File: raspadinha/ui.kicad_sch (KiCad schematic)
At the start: 11 parts, among them Q2 BC338, SW1 RotaryEncoder_Switch

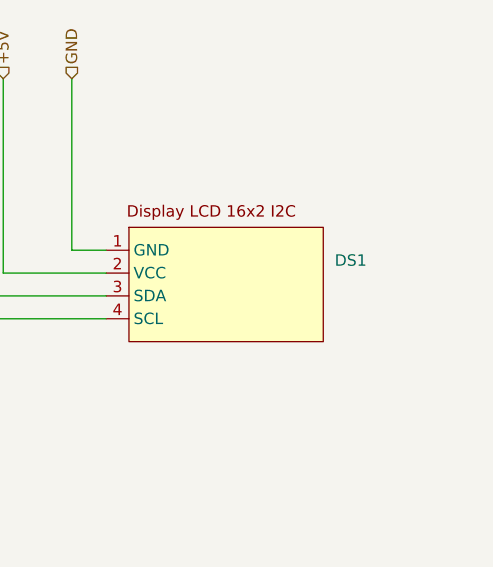
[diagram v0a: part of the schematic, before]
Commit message: feat: usando o mosfet IRFZ44N feat: switch de on/off na fonte de alimentação
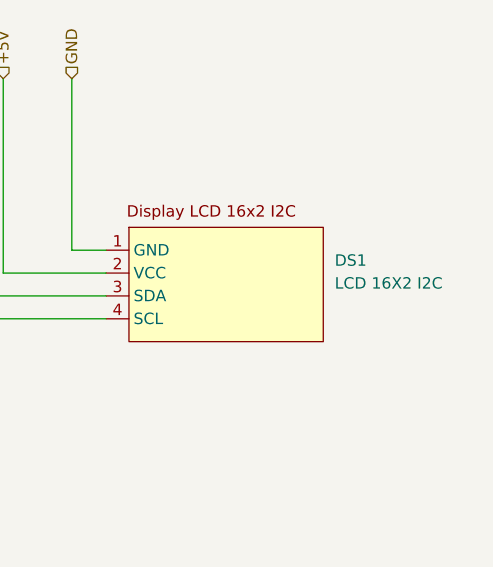
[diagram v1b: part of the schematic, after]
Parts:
- DS1: value ~ -> LCD 16X2 I2C
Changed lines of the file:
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@@
 			)
 		)
-		(property "Value" "~"
+		(property "Value" "LCD 16X2 I2C"
 			(at 248.92 83.6901 0)
 			(effects

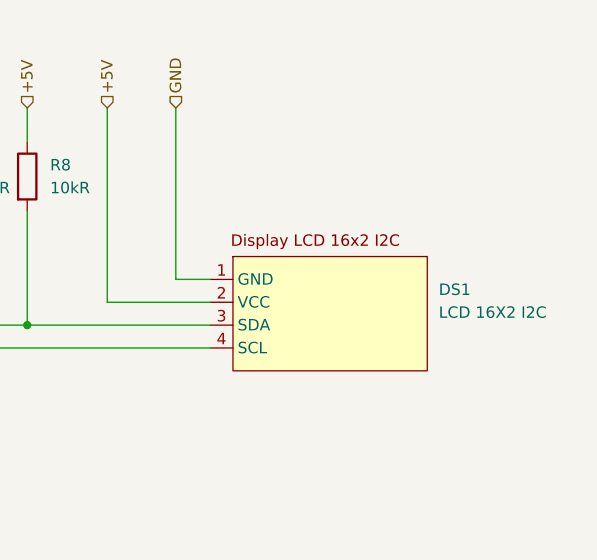
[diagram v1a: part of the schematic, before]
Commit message: feat: Mudança no display utilizado
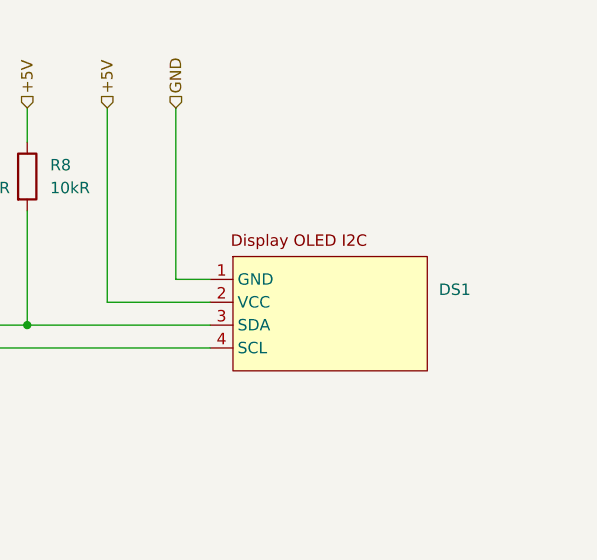
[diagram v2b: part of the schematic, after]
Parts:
- removed DS1: LCD 16X2 I2C, symbol Sorvete:Display_LCD_16x2_I2C
- added DS1: ~, symbol Sorvete:Display_OLED_I2C
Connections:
- net +5V: now also DS1.2 (VCC)
- net DISPLAY_SCL_SIGNAL: now also DS1.3 (SDA)
- net DISPLAY_SDA_SIGNAL: now also DS1.4 (SCL)
- net GND: now also DS1.1 (GND)
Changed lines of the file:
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@@
+	)
+	(symbol
+		(lib_id "Sorvete:Display_OLED_I2C")
+		(at 226.06 76.2 0)
+		(unit 1)
+		(exclude_from_sim no)
+		(in_bom yes)
+		(on_board yes)
+		(dnp no)
+		(fields_autoplaced yes)
+		(property "Reference" "DS1"
+			(at 248.92 81.1501 0)
+			(effects
+				(font
+					(size 1.27 1.27)
+				)
+				(justify left)
+			)
+		)
+		(property "Value" "~"
+			(at 248.92 83.6901 0)
+			(effects
+				(font
+					(size 1.27 1.27)
+				)
+				(justify left)
+			)
+		)
+		(property "Footprint" ""
+			(at 226.06 76.2 0)
+			(effects
+				(font
+					(size 1.27 1.27)
+				)
+				(hide yes)
+			)
+		)
+		(property "Datasheet" ""
+			(at 226.06 76.2 0)
+			(effects
+				(font
+					(size 1.27 1.27)
+				)
+				(hide yes)
+			)
+		)
+		(property "Description" ""
+			(at 226.06 76.2 0)
+			(effects
+				(font
+					(size 1.27 1.27)
+				)
+				(hide yes)
+			)
+		)
+		(pin "4"
+		)
+		(pin "3"
+		)
+		(pin "2"
+		)
+		(pin "1"
+		)
+		(instances
+			(project ""
+				(path "/0ce4bf39-76b0-428c-8682-47e2500753cc/2b8b9fc5-ba35-494d-ab10-49f62bbcd487"
+					(reference "DS1")
+					(unit 1)
+				)
+			)
+		)
 	)
 	(symbol
@@
 					(unit 1)
 				)
-			)
-		)
-	)
-	(symbol
-		(lib_id "Sorvete:Display_LCD_16x2_I2C")
-		(at 226.06 76.2 0)
-		(unit 1)
-		(exclude_from_sim no)
-		(in_bom yes)
-		(on_board yes)
-		(dnp no)
-		(fields_autoplaced yes)
-		(property "Reference" "DS1"
-			(at 248.92 81.1501 0)
-			(effects
-				(font
-					(size 1.27 1.27)
-				)
-				(justify left)
-			)
-		)
-		(property "Value" "LCD 16X2 I2C"
-			(at 248.92 83.6901 0)
-			(effects
-				(font
-					(size 1.27 1.27)
-				)
-				(justify left)
-			)
-		)
-		(property "Footprint" ""
-			(at 226.06 76.2 0)
-			(effects
-				(font
-					(size 1.27 1.27)
-				)
-				(hide yes)
-			)
-		)
-		(property "Datasheet" ""
-			(at 226.06 76.2 0)
-			(effects
-				(font
-					(size 1.27 1.27)
-				)
-				(hide yes)
-			)
-		)
-		(property "Description" ""
-			(at 226.06 76.2 0)
-			(effects
-				(font
-					(size 1.27 1.27)
-				)
-				(hide yes)
-			)
-		)
-		(pin "2"
-		)
-		(pin "3"
-		)
-		(pin "4"
-		)
-		(pin "1"
-		)
-		(instances
-			(project "raspadinha"
-				(path "/0ce4bf39-76b0-428c-8682-47e2500753cc/2b8b9fc5-ba35-494d-ab10-49f62bbcd487"
-					(reference "DS1")
-					(unit 1)
-				)

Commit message: feat: Os Footprint foram todos atribuidos fix: A placa da Esp32 foi trocada pela que temos disponível
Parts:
- BZ1: footprint (none) -> Buzzer_Beeper:MagneticBuzzer_ProSignal_ABT-410-RC
- DS1: footprint (none) -> Connector_PinHeader_2.54mm:PinHeader_1x04_P2.54mm_Vertical
- Q2: footprint (none) -> Package_TO_SOT_THT:TO-92_Inline
- R10, R11, R12, R13, R7, R8, R9: footprint (none) -> Resistor_THT:R_Axial_DIN0411_L9.9mm_D3.6mm_P12.70mm_Horizontal
- SW1: footprint (none) -> Connector_PinHeader_2.54mm:PinHeader_1x05_P2.54mm_Vertical
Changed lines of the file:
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@@
 		(title "Geladinho, UI")
 		(date "2025-11-20")
-		(rev "v1.0.0")
+		(rev "v1.1.0")
 		(company "Universidade Federal Do Ceará")
 	)
@@
 			)
 		)
-		(property "Footprint" ""
+		(property "Footprint" "Resistor_THT:R_Axial_DIN0411_L9.9mm_D3.6mm_P12.70mm_Horizontal"
 			(at 143.51 135.128 90)
 			(effects
@@
 			)
 		)
-		(property "Footprint" ""
+		(property "Footprint" "Connector_PinHeader_2.54mm:PinHeader_1x04_P2.54mm_Vertical"
 			(at 226.06 76.2 0)
 			(effects
@@
 			)
 		)
-		(property "Footprint" ""
+		(property "Footprint" "Resistor_THT:R_Axial_DIN0411_L9.9mm_D3.6mm_P12.70mm_Horizontal"
 			(at 201.422 68.58 90)
 			(effects
@@
 			)
 		)
-		(property "Footprint" ""
+		(property "Footprint" "Resistor_THT:R_Axial_DIN0411_L9.9mm_D3.6mm_P12.70mm_Horizontal"
 			(at 192.532 68.58 90)
 			(effects
@@
 			)
 		)
-		(property "Footprint" ""
+		(property "Footprint" "Package_TO_SOT_THT:TO-92_Inline"
 			(at 162.56 135.255 0)
 			(effects
@@
 			)
 		)
-		(property "Footprint" ""
+		(property "Footprint" "Resistor_THT:R_Axial_DIN0411_L9.9mm_D3.6mm_P12.70mm_Horizontal"
 			(at 132.842 142.24 90)
 			(effects
@@
 			)
 		)
-		(property "Footprint" ""
+		(property "Footprint" "Connector_PinHeader_2.54mm:PinHeader_1x05_P2.54mm_Vertical"
 			(at 93.98 78.486 0)
 			(effects
@@
 			)
 		)
-		(property "Footprint" ""
+		(property "Footprint" "Buzzer_Beeper:MagneticBuzzer_ProSignal_ABT-410-RC"
 			(at 161.925 116.84 90)
 			(effects
@@
 			)
 		)
-		(property "Footprint" ""
+		(property "Footprint" "Resistor_THT:R_Axial_DIN0411_L9.9mm_D3.6mm_P12.70mm_Horizontal"
 			(at 76.962 68.58 90)
 			(effects
@@
 			)
 		)
-		(property "Footprint" ""
+		(property "Footprint" "Resistor_THT:R_Axial_DIN0411_L9.9mm_D3.6mm_P12.70mm_Horizontal"
 			(at 66.802 68.58 90)
 			(effects
@@
 			)
 		)
-		(property "Footprint" ""
+		(property "Footprint" "Resistor_THT:R_Axial_DIN0411_L9.9mm_D3.6mm_P12.70mm_Horizontal"
 			(at 108.712 92.71 90)
 			(effects

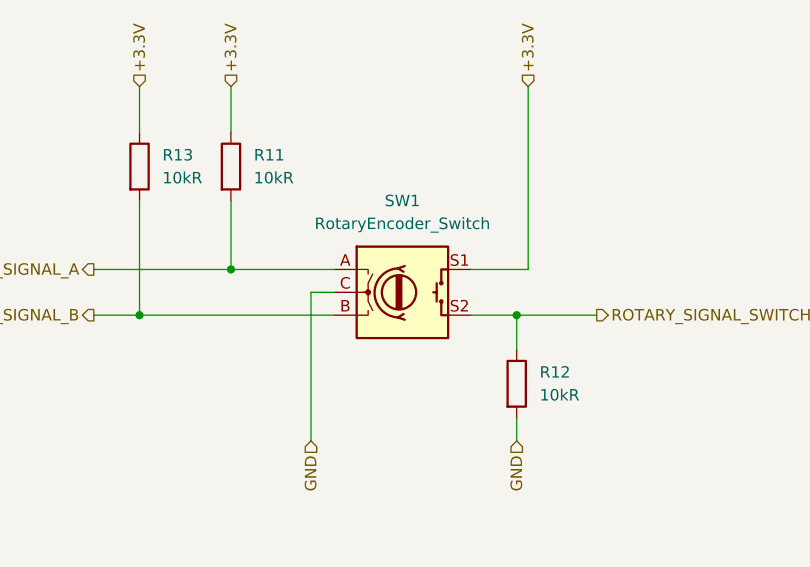
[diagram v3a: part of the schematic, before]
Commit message: feat: Posicionamento dos componentes na placa
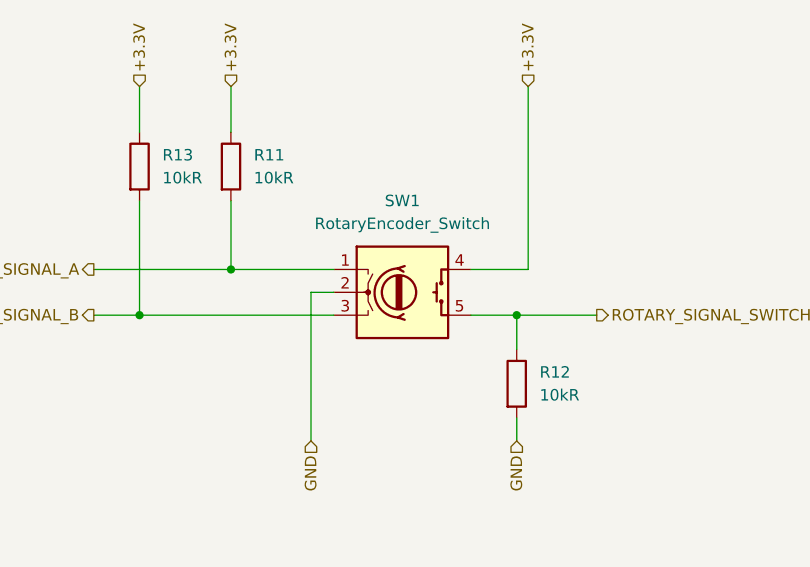
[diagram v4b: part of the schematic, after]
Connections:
- net +3.3V: now also SW1.4 (S1); no longer SW1.S1
- net GND: now also SW1.2 (C); no longer SW1.C
- net ROTARY_SIGNAL_A: now also SW1.1 (A); no longer SW1.A
- net ROTARY_SIGNAL_B: now also SW1.3 (B); no longer SW1.B
- net ROTARY_SIGNAL_SWITCH: now also SW1.5 (S2); no longer SW1.S2
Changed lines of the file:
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@@
 			)
 		)
-		(pin "C"
+		(pin "1"
 		)
-		(pin "A"
+		(pin "3"
 		)
-		(pin "S2"
+		(pin "4"
 		)
-		(pin "S1"
+		(pin "2"
 		)
-		(pin "B"
+		(pin "5"
 		)
 		(instances

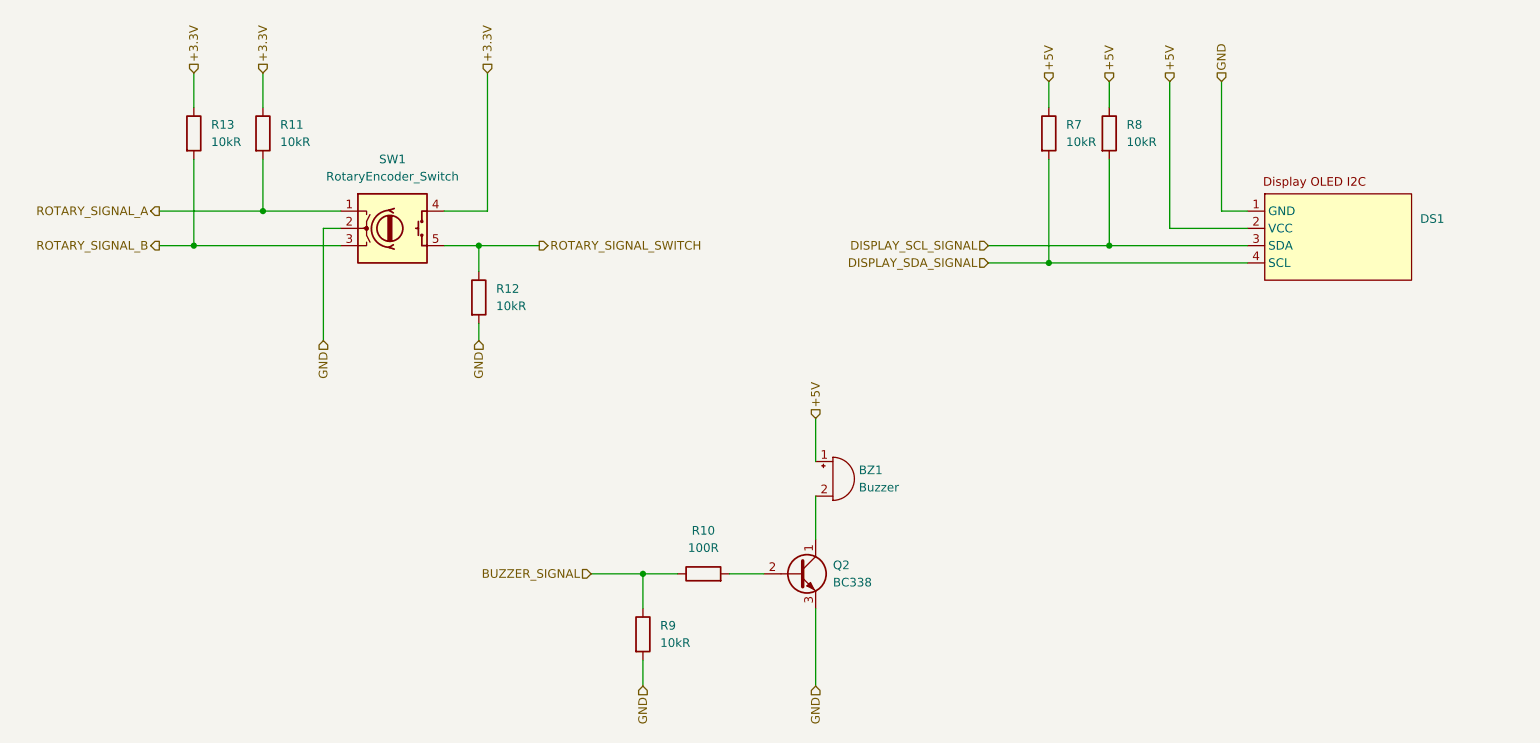
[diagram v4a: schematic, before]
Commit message: feat: Refatoração da alimentação da placa feat: Renomeação do número dos componentes
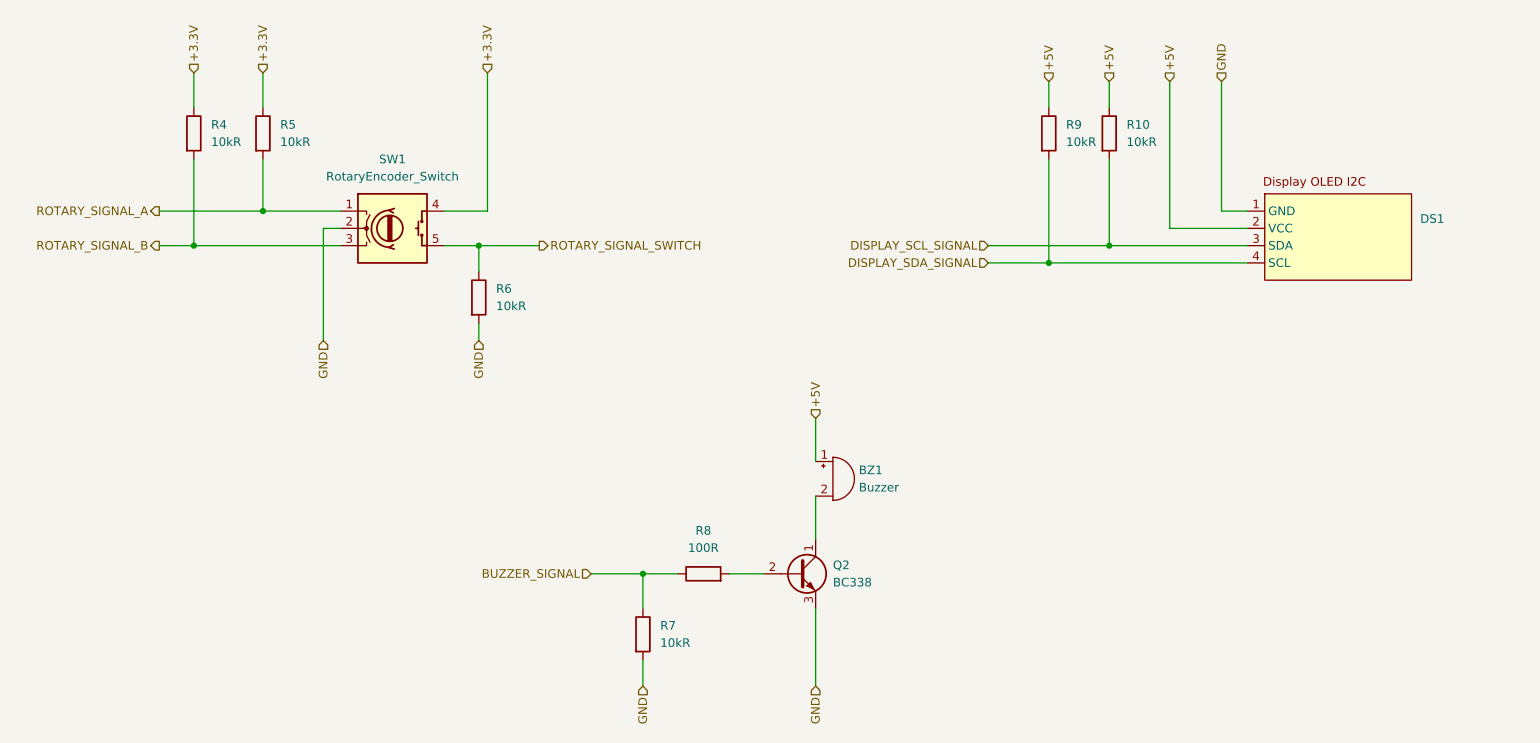
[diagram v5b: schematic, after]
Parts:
- renumbered R8 to R10, R13 to R4, R11 to R5, R12 to R6, R9 to R7, R10 to R8, R7 to R9
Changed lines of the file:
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@@
 		(dnp no)
 		(fields_autoplaced yes)
-		(property "Reference" "R10"
+		(property "Reference" "R8"
 			(at 143.51 127 90)
 			(effects
@@
 			(project "raspadinha"
 				(path "/0ce4bf39-76b0-428c-8682-47e2500753cc/2b8b9fc5-ba35-494d-ab10-49f62bbcd487"
-					(reference "R10")
+					(reference "R8")
 					(unit 1)
 				)
@@
 		(dnp no)
 		(fields_autoplaced yes)
-		(property "Reference" "R8"
+		(property "Reference" "R10"
 			(at 205.74 67.3099 0)
 			(effects
@@
 			(project "raspadinha"
 				(path "/0ce4bf39-76b0-428c-8682-47e2500753cc/2b8b9fc5-ba35-494d-ab10-49f62bbcd487"
-					(reference "R8")
+					(reference "R10")
 					(unit 1)
 				)
@@
 		(dnp no)
 		(fields_autoplaced yes)
-		(property "Reference" "R7"
+		(property "Reference" "R9"
 			(at 196.85 67.3099 0)
 			(effects
@@
 			(project "raspadinha"
 				(path "/0ce4bf39-76b0-428c-8682-47e2500753cc/2b8b9fc5-ba35-494d-ab10-49f62bbcd487"
-					(reference "R7")
+					(reference "R9")
 					(unit 1)
 				)
@@
 		(dnp no)
 		(fields_autoplaced yes)
-		(property "Reference" "R9"
+		(property "Reference" "R7"
 			(at 137.16 140.9699 0)
 			(effects
@@
 			(project "raspadinha"
 				(path "/0ce4bf39-76b0-428c-8682-47e2500753cc/2b8b9fc5-ba35-494d-ab10-49f62bbcd487"
-					(reference "R9")
+					(reference "R7")
 					(unit 1)
 				)
@@
 		(dnp no)
 		(fields_autoplaced yes)
-		(property "Reference" "R11"
+		(property "Reference" "R5"
 			(at 81.28 67.3099 0)
 			(effects
@@
 			(project "raspadinha"
 				(path "/0ce4bf39-76b0-428c-8682-47e2500753cc/2b8b9fc5-ba35-494d-ab10-49f62bbcd487"
-					(reference "R11")
+					(reference "R5")
 					(unit 1)
 				)
@@
 		(dnp no)
 		(fields_autoplaced yes)
-		(property "Reference" "R13"
+		(property "Reference" "R4"
 			(at 71.12 67.3099 0)
 			(effects
@@
 			(project "raspadinha"
 				(path "/0ce4bf39-76b0-428c-8682-47e2500753cc/2b8b9fc5-ba35-494d-ab10-49f62bbcd487"
-					(reference "R13")
+					(reference "R4")
 					(unit 1)
 				)
@@
 		(dnp no)
 		(fields_autoplaced yes)
-		(property "Reference" "R12"
+		(property "Reference" "R6"
 			(at 113.03 91.4399 0)
 			(effects
@@
 			(project "raspadinha"
 				(path "/0ce4bf39-76b0-428c-8682-47e2500753cc/2b8b9fc5-ba35-494d-ab10-49f62bbcd487"
-					(reference "R12")
-					(unit 1)
-				)
+					(reference "R6")
+					(unit 1)
+				)
